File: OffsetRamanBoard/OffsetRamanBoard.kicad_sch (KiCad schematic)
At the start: 25 parts, among them J1 RJ45_LED_Shielded, J2 XLR3, J4 NC4FBH, Q1 BSS138, U1 Teensy4.1_DEV-16771, U2 LM317_TO-220, U3 OKI, U5 D36V28F7, U6 TMC2208

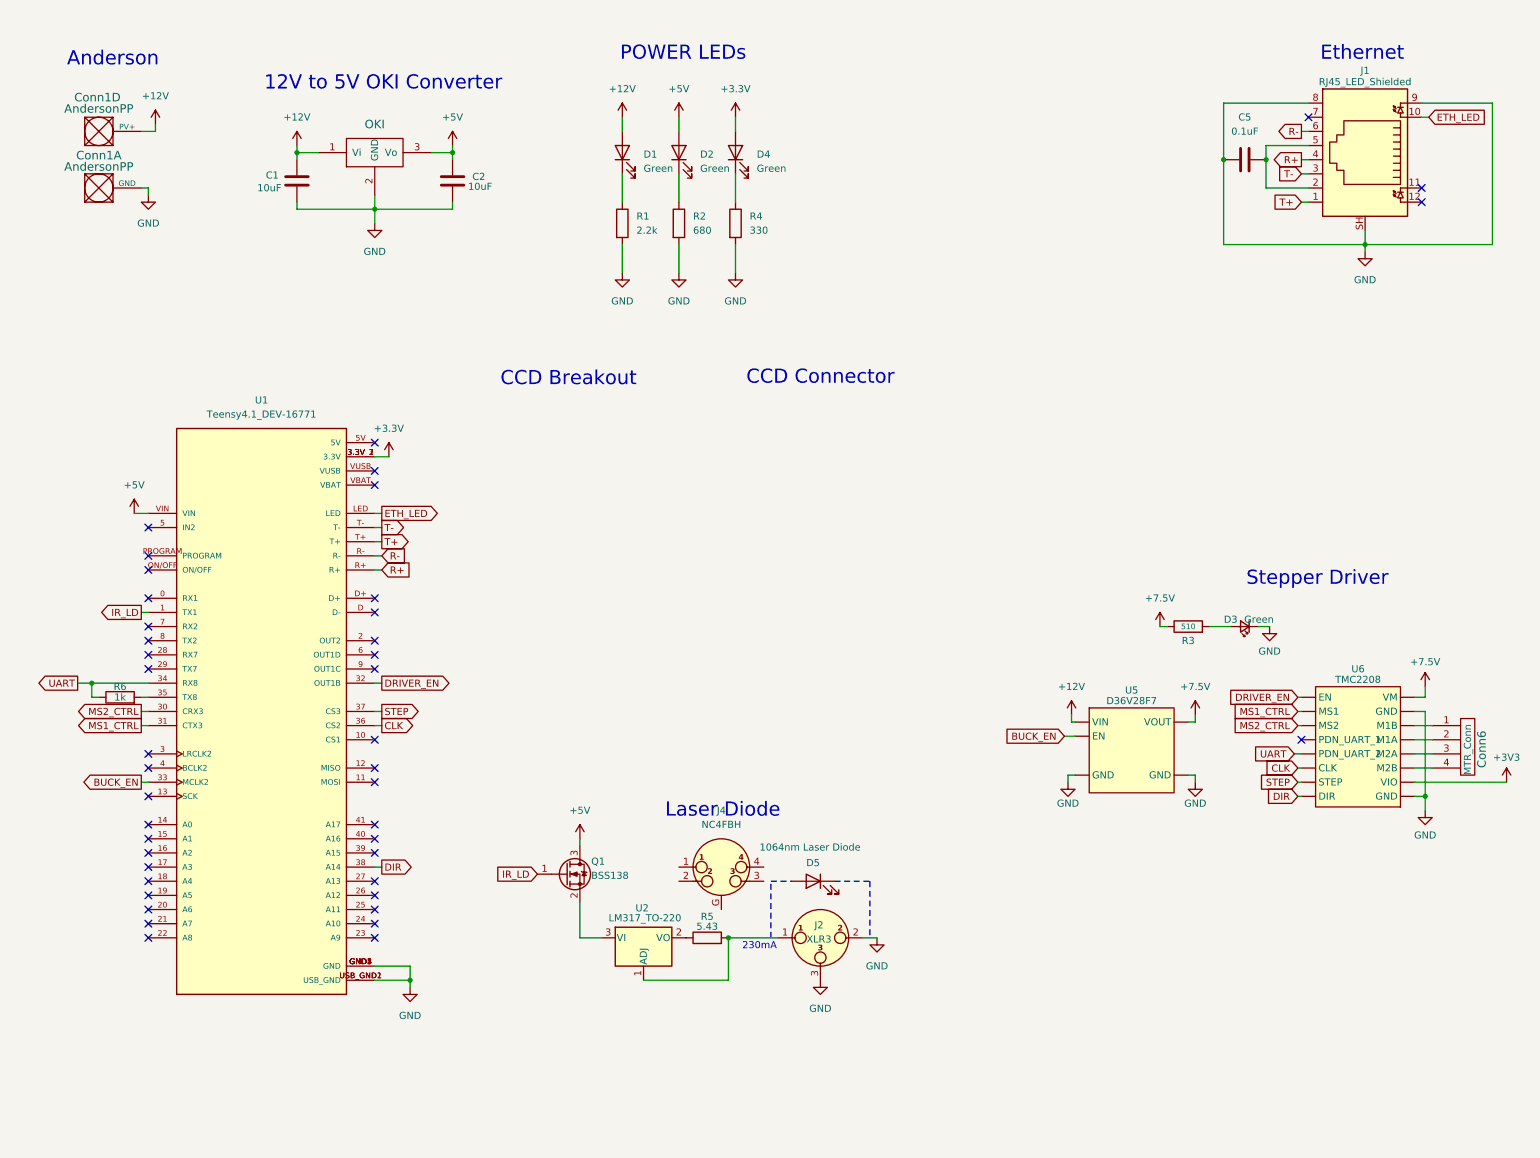
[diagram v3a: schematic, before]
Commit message: Rearranged Schematic And Updated Resistor Value
Rearraged the different sections in the schematic and made them each more compact. I also added the calculated feedback resistor value to the transimpedance amplifier.
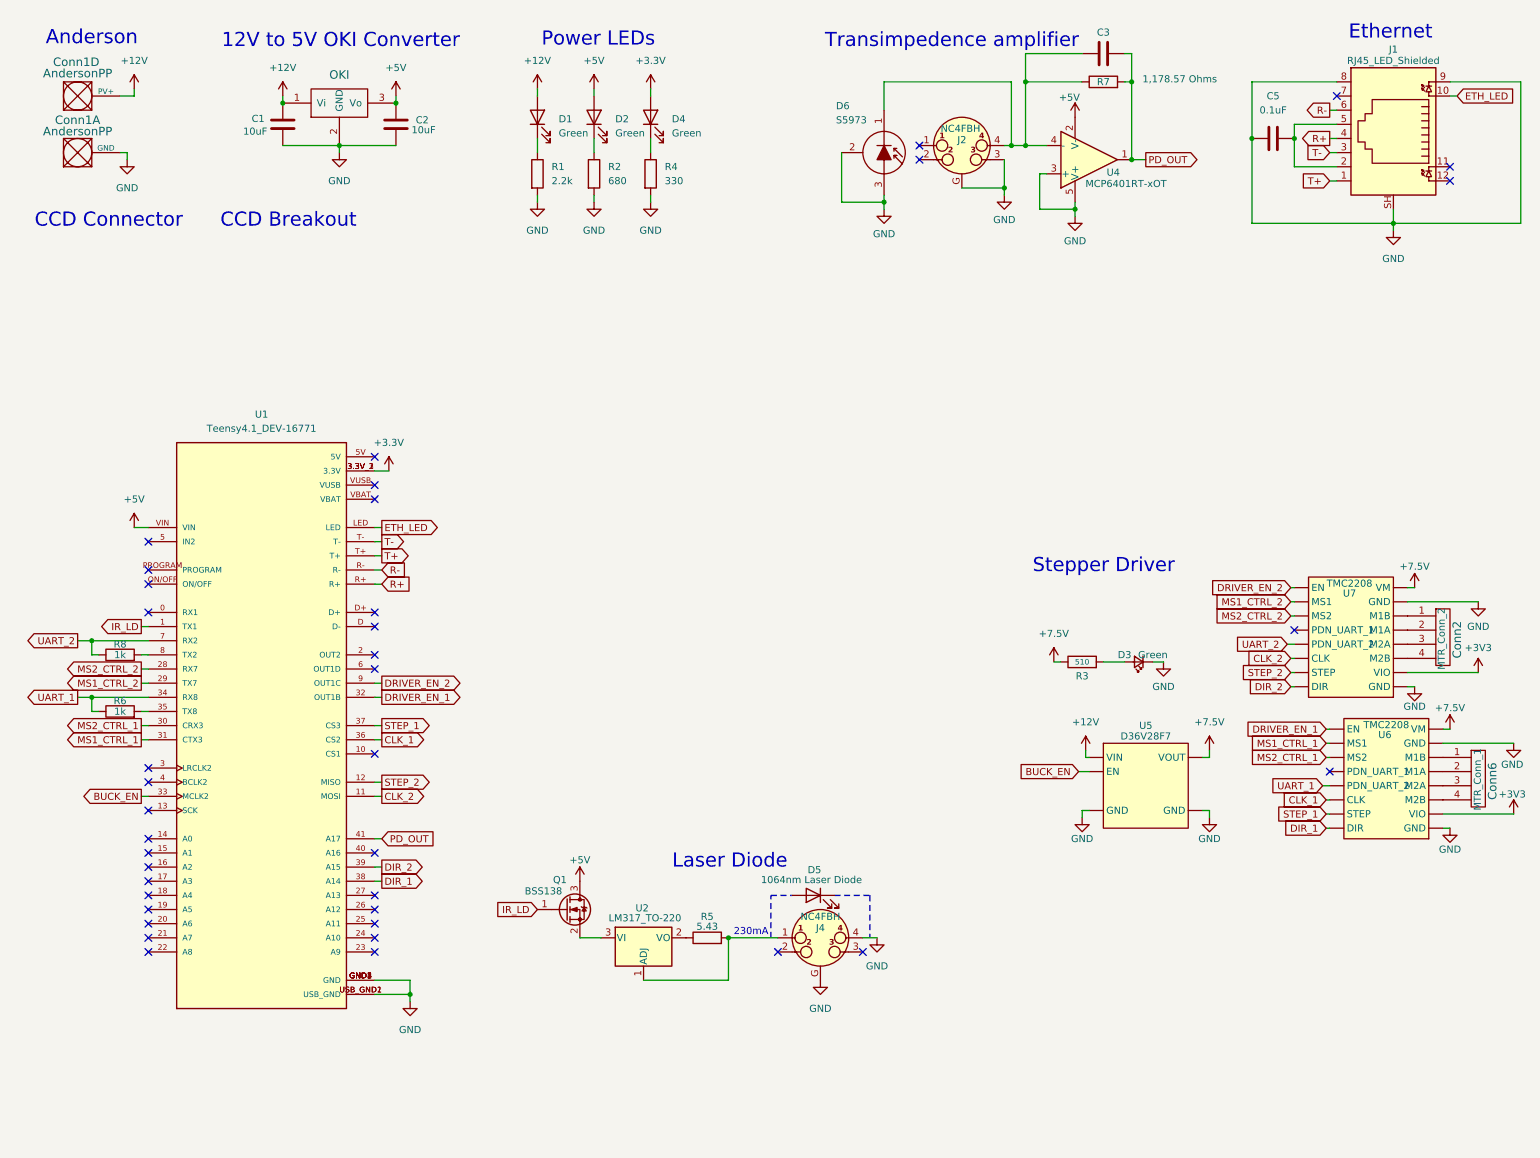
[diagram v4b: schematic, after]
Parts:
- removed J2: XLR3, symbol Connector_Audio:XLR3
- added C3: ~, Capacitor_SMD:C_0603_1608Metric_Pad1.08x0.95mm_HandSolder, symbol Device:C
- added Conn2: MTR_Conn_2, MRDT_Connectors:MOLEX_SL_04_Vertical, symbol MRDT_Connectors:Molex_SL_04
- added D6: S5973, Package_TO_SOT_THT:TO-18-3, symbol Sensor_Optical:S5973
- added J2: NC4FBH, Connector_Audio:Jack_XLR_Neutrik_NC4FBH_Horizontal, symbol Connector_Audio:NC4FBH
- added R7: 1,178.57 Ohms, Resistor_SMD:R_0603_1608Metric_Pad0.98x0.95mm_HandSolder, symbol Device:R
- added R8: 1k, Resistor_SMD:R_0603_1608Metric_Pad0.98x0.95mm_HandSolder, symbol Device:R
- added U4: MCP6401RT-xOT, Package_TO_SOT_SMD:SOT-23-5, symbol Amplifier_Operational:MCP6401RT-xOT
- added U7: TMC2208, FTIR_Footprints:MODULE_TMC2208_SILENTSTEPSTICK, symbol Stepper_Driver_Headers:TMC2208_Breakout
- Conn6: value MTR_Conn -> MTR_Conn_1
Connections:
- net +3V3: now also U7.VIO
- net +5V: now also U4.2 (V-)
- net +7.5V: now also U7.VM
- net GND: now also J4.4, J4.G, D6.2 (C), D6.3 (A), J2.3, J2.G, U4.3 (+), U4.5 (V+), U7.GND
- net at J4.1: now also R5.2, U2.1 (ADJ)
- net CLK_2: now reaches U1.11 (MOSI)
- net CLK_2: now also U7.CLK
- net STEP_2: now reaches U1.12 (MISO)
- net STEP_2: now also U7.STEP
- net MS2_CTRL_2: now reaches U1.28 (RX7)
- net MS2_CTRL_2: now also U7.MS2
- net MS1_CTRL_2: now reaches U1.29 (TX7)
- net MS1_CTRL_2: now also U7.MS1
- net DIR_2: now reaches U1.39 (A15)
- net DIR_2: now also U7.DIR
- net PD_OUT: now reaches U1.41 (A17)
- net PD_OUT: now also C3.1, R7.2, U4.1
- net UART_2: now reaches U1.7 (RX2)
- net UART_2: now also R8.1, U7.PDN_UART_2
- net at U1.8 (TX2): now also R8.2
- net DRIVER_EN_2: now reaches U1.9 (OUT1C)
- net DRIVER_EN_2: now also U7.EN
- net CLK renamed CLK_1
- net DIR renamed DIR_1
- net DRIVER_EN renamed DRIVER_EN_1
- net MS1_CTRL renamed MS1_CTRL_1
- net MS2_CTRL renamed MS2_CTRL_1
- net STEP renamed STEP_1
- net UART renamed UART_1
- new net: C3.2, D6.1 (K), J2.4, R7.1, U4.4 (-)
- new net: Conn2.2, U7.M1A
- new net: Conn2.1, U7.M1B
- new net: Conn2.3, U7.M2A
- new net: Conn2.4, U7.M2B
- no-connect marks 43 -> 39
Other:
- note added: "Power LEDs"
- note added: "Transimpedence amplifier"
- note removed: "POWER LEDs"
- moved on the sheet: C1, C2, C5, Conn1A, Conn1D, Conn6, D1, D2, D3, D4, D5, J1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

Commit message: Rearranged schematic
Made it more compact and added separation lines.
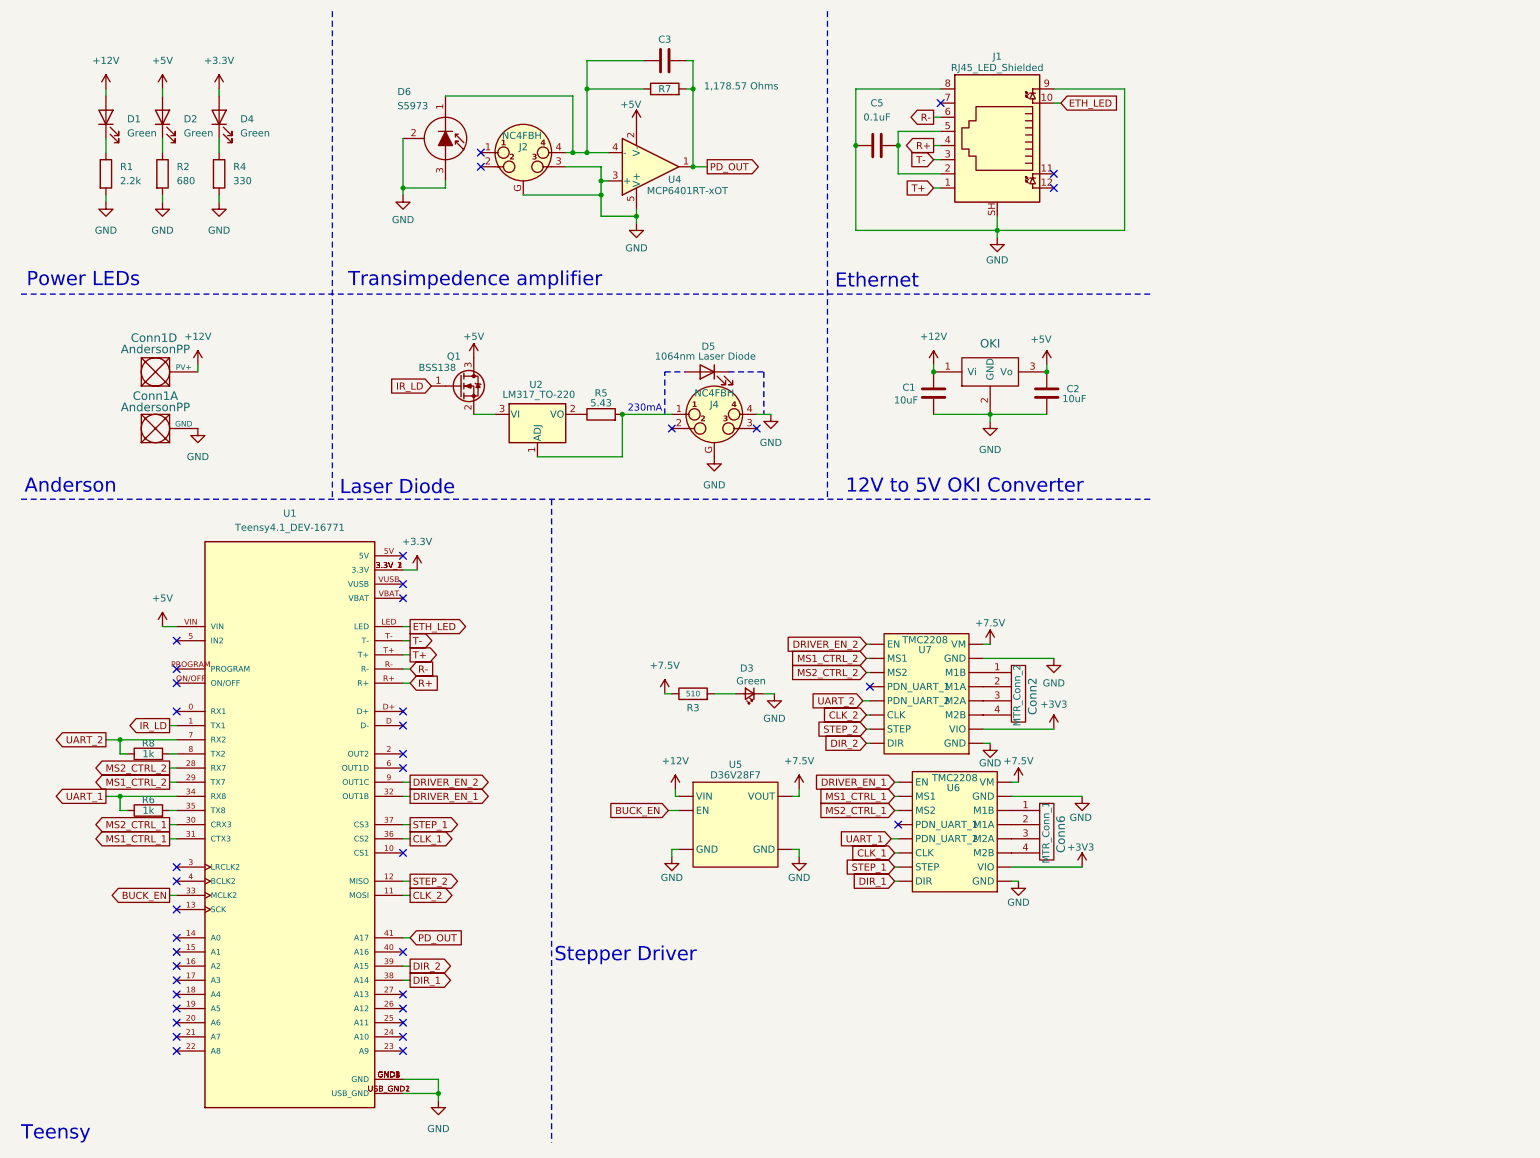
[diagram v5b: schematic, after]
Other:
- note added: "Teensy"
- note removed: "CCD Breakout"
- note removed: "CCD Connector"
- moved on the sheet: C1, C2, C3, C5, Conn1A, Conn1D, Conn2, Conn6, D1, D2, D3, D4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

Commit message: Removed Photodiode circuits and extra motor.
Deleted the transimpedance amplifier, as well as the extra stepper motor driver board with its respective input and output pins that connected to the teensy.
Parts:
- removed C3: ~, Capacitor_SMD:C_0603_1608Metric_Pad1.08x0.95mm_HandSolder, symbol Device:C
- removed Conn2: MTR_Conn_2, MRDT_Connectors:MOLEX_SL_04_Vertical, symbol MRDT_Connectors:Molex_SL_04
- removed D6: S5973, Package_TO_SOT_THT:TO-18-3, symbol Sensor_Optical:S5973
- removed J2: NC4FBH, Connector_Audio:Jack_XLR_Neutrik_NC4FBH_Horizontal, symbol Connector_Audio:NC4FBH
- removed R7: 1,178.57 Ohms, Resistor_SMD:R_0603_1608Metric_Pad0.98x0.95mm_HandSolder, symbol Device:R
- removed R8: 1k, Resistor_SMD:R_0603_1608Metric_Pad0.98x0.95mm_HandSolder, symbol Device:R
- removed U4: MCP6401RT-xOT, Package_TO_SOT_SMD:SOT-23-5, symbol Amplifier_Operational:MCP6401RT-xOT
- removed U7: TMC2208, FTIR_Footprints:MODULE_TMC2208_SILENTSTEPSTICK, symbol Stepper_Driver_Headers:TMC2208_Breakout
- added Conn3: Molex_SL_05, MRDT_Connectors:MOLEX_SL_05_Vertical, symbol MRDT_Connectors:Molex_SL_05
- added Q2, Q3: BSS138, Package_TO_SOT_SMD:SOT-23, symbol Transistor_FET:BSS138
- added R10, R9: 4.7k, Resistor_SMD:R_0603_1608Metric_Pad0.98x0.95mm_HandSolder, symbol Device:R
- D5: value 1064nm Laser Diode -> 840nm Laser Diode
- R5: value 5.43 -> 4.9
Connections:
- net +3V3: now also Q2.1 (G), Q3.1 (G)
- net +5V: now also Conn3.1, R10.1, R9.1
- net GND: now also Conn3.5
- net CCD_ROG_3V3: now reaches U1.24 (A10)
- net CCD_ROG_3V3: now also Q2.2 (S)
- net CLD_CLK_3V3: now reaches U1.25 (A11)
- net CLD_CLK_3V3: now also Q3.2 (S)
- net CCD_Vout: now reaches U1.26 (A12)
- net CCD_Vout: now also Conn3.2
- net DIR_2: no longer names the net of U1.39 (A15)
- net DRIVER_EN_2: no longer names the net of U1.9 (OUT1C)
- net MS1_CTRL_2: no longer names the net of U1.29 (TX7)
- net MS2_CTRL_2: no longer names the net of U1.28 (RX7)
- net STEP_2: no longer names the net of U1.12 (MISO)
- net UART_2: no longer names the net of U1.7 (RX2)
- new net CCD_CLK_5V: Conn3.4, Q3.3 (D), R10.2
- new net CCD_ROG_5V: Conn3.3, Q2.3 (D), R9.2
- no-connect marks 39 -> 40
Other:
- note added: "255mA"
- note added: "CCD Breakout"
- note added: "CCD Clocks"
- note removed: "230mA"
- note removed: "Transimpedence amplifier"
- moved on the sheet: Conn1A, Conn1D, Conn6, D1, D2, D3, D4, D5, J4, Q1, R1, R2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

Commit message: Updated to be photodiode compatible
Added a second stepper motor controller, added a transimpedance amplifier circuit, removed CCD Breakout connectors, and removed CCD clocks.
Resistor and capacitor values for the TIA circuit are not up to date, and the laser diode wavelength and its respective current limit may not be up to date either.
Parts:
- removed Conn3: Molex_SL_05, MRDT_Connectors:MOLEX_SL_05_Vertical, symbol MRDT_Connectors:Molex_SL_05
- removed Q2, Q3: BSS138, Package_TO_SOT_SMD:SOT-23, symbol Transistor_FET:BSS138
- removed R10, R9: 4.7k, Resistor_SMD:R_0603_1608Metric_Pad0.98x0.95mm_HandSolder, symbol Device:R
- added C3: C, symbol Device:C
- added Conn2: MTR_Conn_1, MRDT_Connectors:MOLEX_SL_04_Vertical, symbol MRDT_Connectors:Molex_SL_04
- added D6: S5973, Package_TO_SOT_THT:TO-18-3, symbol Sensor_Optical:S5973
- added J2: NC4FBH, Connector_Audio:Jack_XLR_Neutrik_NC4FBH_Horizontal, symbol Connector_Audio:NC4FBH
- added R7: 1k, Resistor_SMD:R_0603_1608Metric_Pad0.98x0.95mm_HandSolder, symbol Device:R
- added R8: 1,178.57 Ohms, symbol Device:R
- added U4: TMC2208, FTIR_Footprints:MODULE_TMC2208_SILENTSTEPSTICK, symbol Stepper_Driver_Headers:TMC2208_Breakout
- added U7: MCP6401RT-xOT, Package_TO_SOT_SMD:SOT-23-5, symbol Amplifier_Operational:MCP6401RT-xOT
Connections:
- net +3V3: now also U4.VIO
- net +5V: now also U7.2 (V-)
- net +7.5V: now also U4.VM
- net CLK_2: now also U4.CLK
- net GND: now also D6.2 (C), D6.3 (A), J2.3, J2.G, U4.GND, U7.3 (+), U7.5 (V+)
- net PD_OUT: now also C3.1, R8.2, U7.1
- net STEP_2: now reaches U1.12 (MISO)
- net STEP_2: now also U4.STEP
- net MS2_CTRL_2: now reaches U1.28 (RX7)
- net MS2_CTRL_2: now also U4.MS2
- net MS1_CTRL_2: now reaches U1.29 (TX7)
- net MS1_CTRL_2: now also U4.MS1
- net DIR_2: now reaches U1.39 (A15)
- net DIR_2: now also U4.DIR
- net UART_2: now reaches U1.7 (RX2)
- net UART_2: now also R7.1, U4.PDN_UART_2
- net at U1.8 (TX2): now also R7.2
- net DRIVER_EN_2: now reaches U1.9 (OUT1C)
- net DRIVER_EN_2: now also U4.EN
- net CCD_ROG_3V3: no longer names the net of U1.24 (A10)
- net CCD_Vout: no longer names the net of U1.26 (A12)
- net CLD_CLK_3V3: no longer names the net of U1.25 (A11)
- new net: Conn2.2, U4.M1A
- new net: Conn2.1, U4.M1B
- new net: Conn2.3, U4.M2A
- new net: Conn2.4, U4.M2B
- new net: C3.2, D6.1 (K), J2.4, R8.1, U7.4 (-)
- no-connect marks 40 -> 37
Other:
- note added: "Transimpedence amplifier"
- note removed: "CCD Breakout"
- note removed: "CCD Clocks"
- moved on the sheet: Conn6, D3, R3, U5, U6
